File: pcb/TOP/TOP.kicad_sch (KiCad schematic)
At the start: 27 parts, among them J1 Conn_01x04, SW100 SW_DPDT_x2, SW101 SW_DPDT_x2, SW102 SW_SPDT, SW103 SW_SPDT, SW200 SW_DPDT_x2, SW201 SW_DPDT_x2, SW202 SW_SPDT, SW203 SW_SPDT

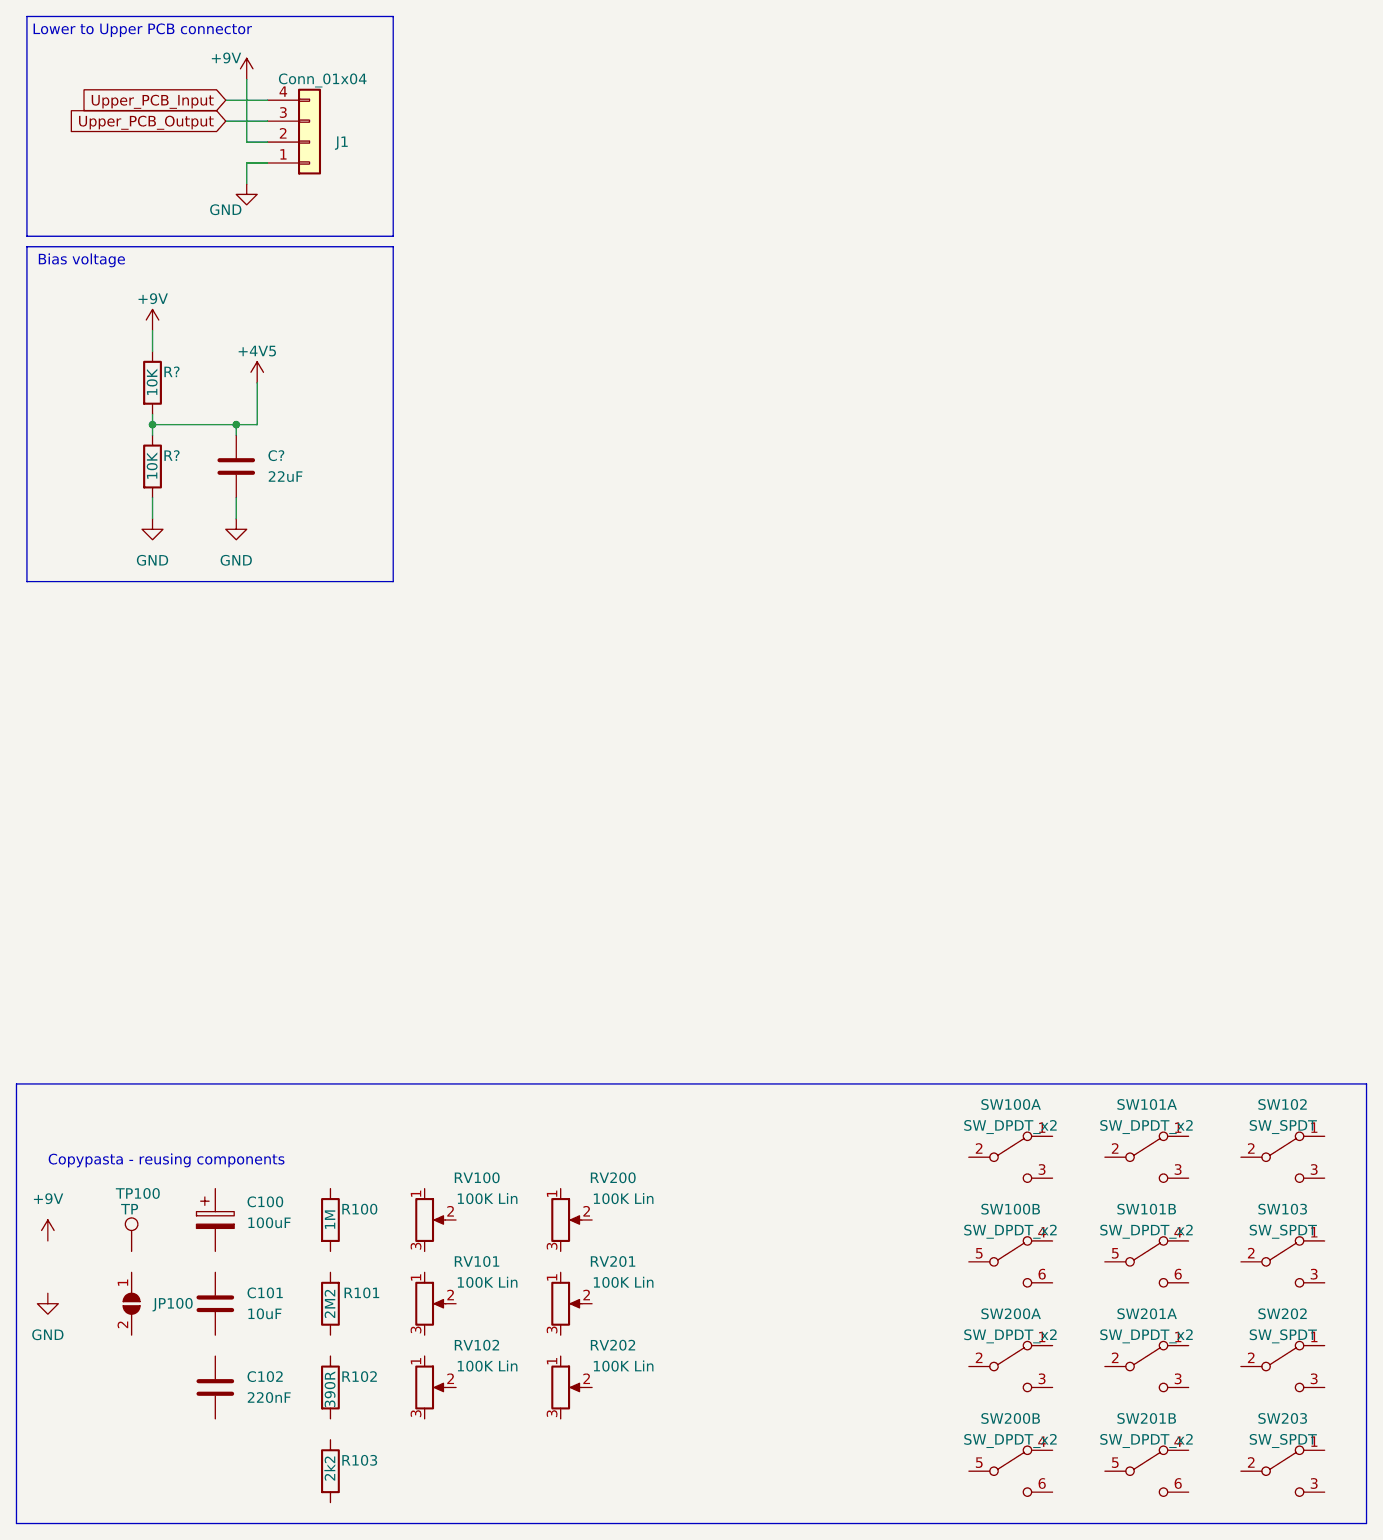
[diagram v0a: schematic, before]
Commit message: [TOP] Start schematic while debating the layout
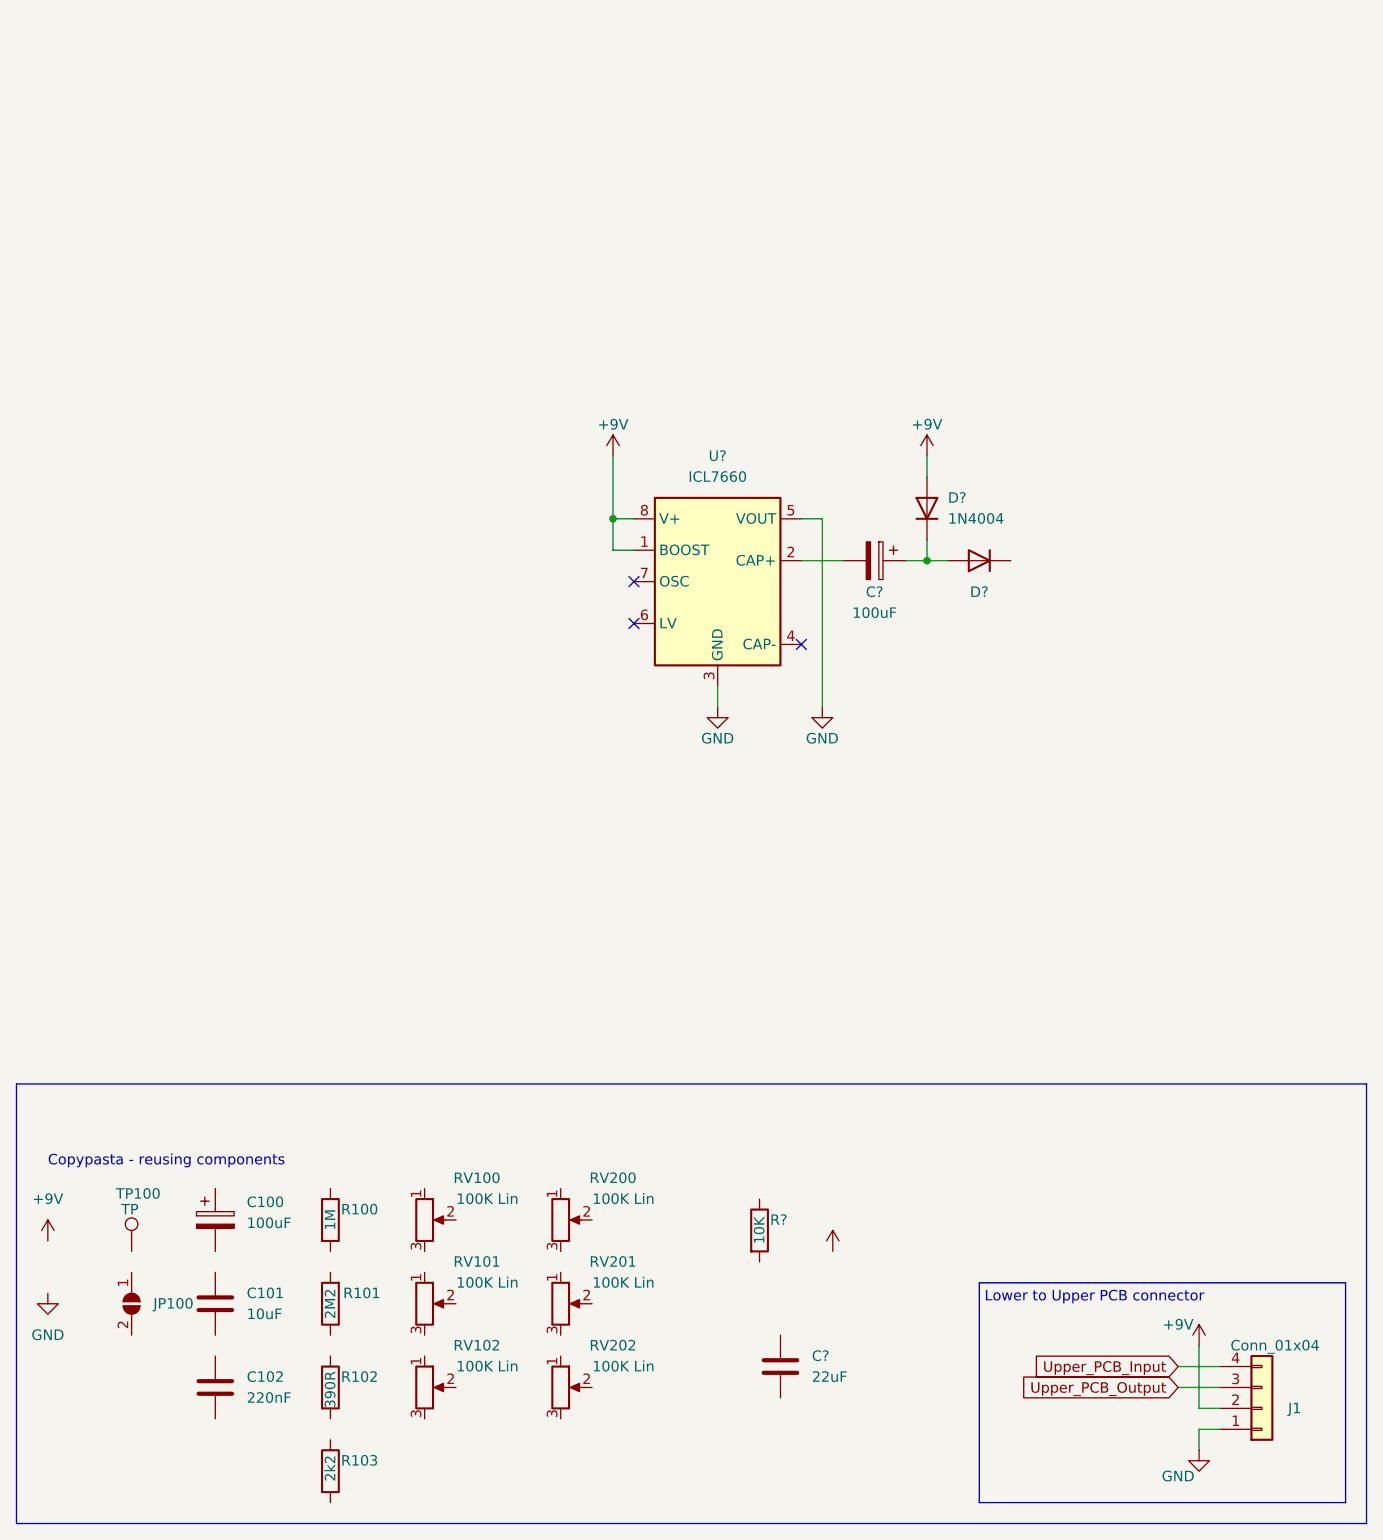
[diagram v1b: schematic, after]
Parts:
- removed R?: 10K, Resistor_SMD:R_0603_1608Metric, symbol Device:R
- removed SW100, SW101, SW200, SW201: SW_DPDT_x2, MeineBib:Switch_toggle_DPDT_Print, symbol Switch:SW_DPDT_x2
- removed SW102, SW103, SW202, SW203: SW_SPDT, MeineBib:Switch_toggle_SPDT_Print, symbol Switch:SW_SPDT
- added C?: 100uF, Capacitor_THT:CP_Radial_D5.0mm_P2.00mm, symbol Device:C_Polarized
- added D?: 1N4004, Diode_THT:D_DO-41_SOD81_P10.16mm_Horizontal, symbol Diode:1N4004
- added D?: (no value), symbol Diode:1N4004
- added U?: ICL7660, symbol Regulator_SwitchedCapacitor:ICL7660
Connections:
- net +4V5: no longer C?.1, R?.2
- net +9V: now also D?.2 (A), U?.1 (BOOST), U?.8 (V+); no longer R?.1
- net GND: now also U?.3 (GND), U?.5 (VOUT); no longer C?.2
- new net: C?.1, D?.1 (K), D?.2 (A)
- new net: C?.2, U?.2 (CAP+)
- no-connect marks 0 -> 3
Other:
- note removed: "Bias voltage"
- moved on the sheet: C?, J1, R?

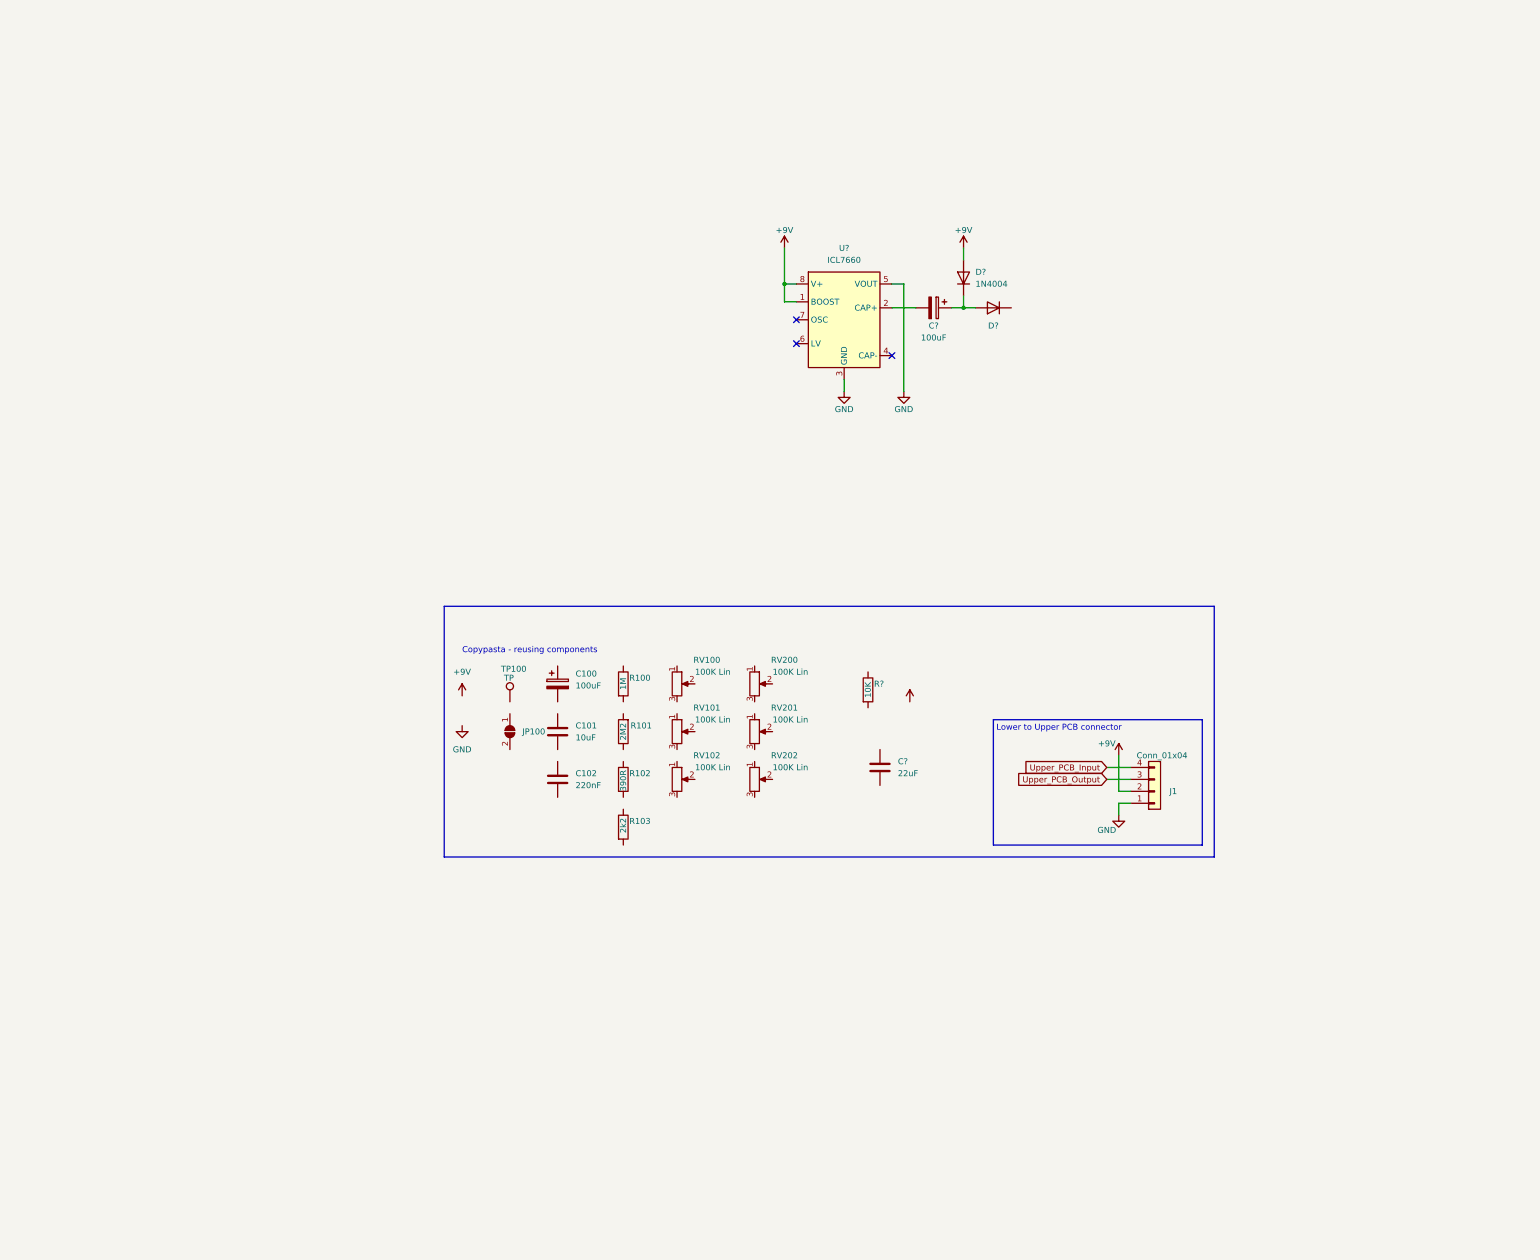
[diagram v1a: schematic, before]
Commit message: [TOP] Draw schematic input and distortion stages
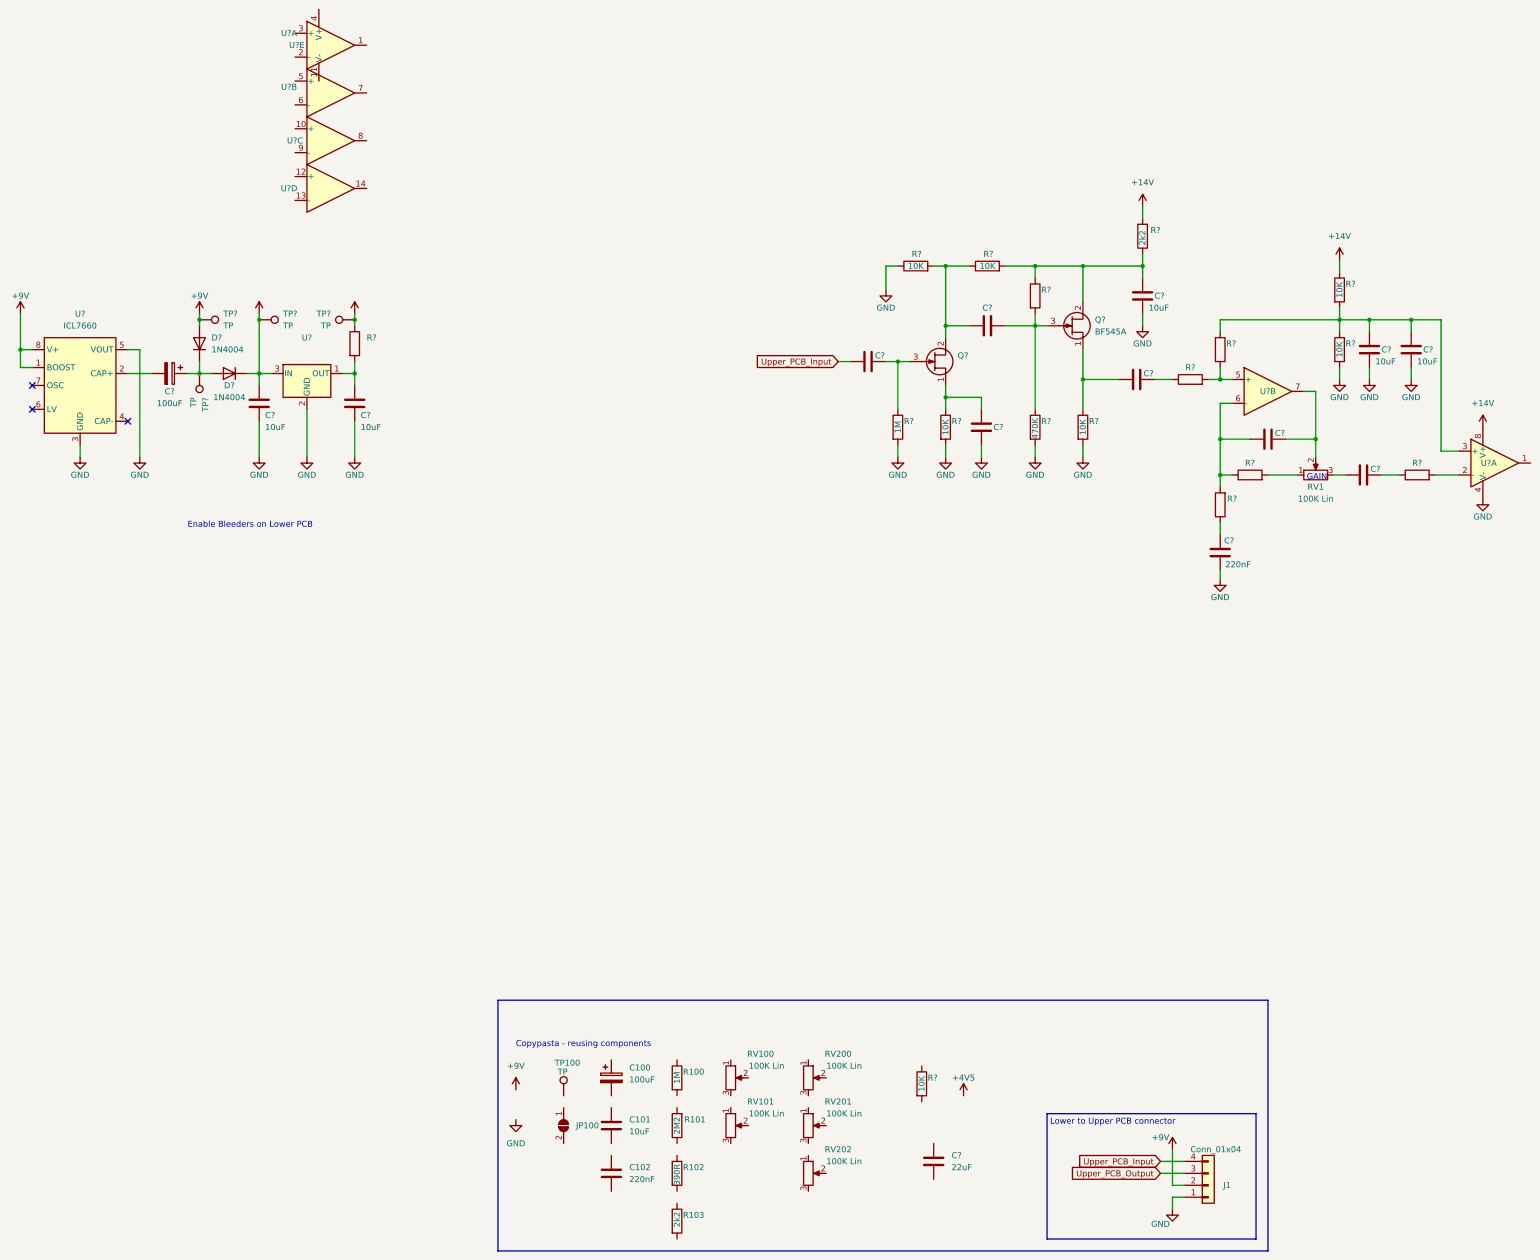
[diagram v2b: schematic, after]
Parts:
- added C? (x5): 10uF, Capacitor_SMD:C_0805_2012Metric, symbol Device:C
- added C? (x6): (no value), symbol Device:C
- added C?: 220nF, symbol Device:C
- added Q?: BF545A, Package_TO_SOT_SMD:SOT-23, symbol Transistor_FET:BF545A
- added Q?: (no value), symbol Transistor_FET:BF545A
- added R? (x7): (no value), symbol Device:R
- added R?: 2k2, Resistor_SMD:R_0603_1608Metric, symbol Device:R
- added R? (x6): 10K, Resistor_SMD:R_0603_1608Metric, symbol Device:R
- added R?: 1M, Resistor_SMD:R_0603_1608Metric, symbol Device:R
- added R?: 470K, symbol Device:R
- added TP? (x4): TP, TestPoint:TestPoint_Pad_D2.0mm, symbol Connector:TestPoint
- added U? (x5): (no value), symbol Amplifier_Operational:TL074
- added U?: (no value), symbol Regulator_Linear:L78L15_SOT89
- added U? (x3): (no value), symbol MeineBibli:OPA2604
- D?: value (none) -> 1N4004; footprint (none) -> Diode_THT:D_DO-41_SOD81_P10.16mm_Horizontal
- renumbered RV102 to RV1
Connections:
- net +4V5: now also D?.1 (K), C?.1, R?.1, R?.1, R?.2, TP?.1, TP?.1, U?.3 (IN), U?.8 (V+)
- net +9V: now also TP?.1
- net GND: now also C?.1, C?.2, C?.2, C?.2, C?.2, C?.2, C?.2, R?.1, R?.2, R?.2, R?.2, R?.2, R?.2, U?.2 (GND), U?.4 (V-)
- net Upper_PCB_Input: now also C?.2
- net at C?.1, D?.1 (K), D?.2 (A): now also TP?.1
- net at RV1.1: now also R?.2
- net at RV1.2: now also C?.1, U?.7
- net at RV1.3: now also C?.2
- new net: C?.1, R?.1 (x2)
- new net: R?.2, U?.2 (-)
- new net: C?.1, Q?.2 (D), R?.1, R?.1, R?.2
- new net: C?.1, Q?.3 (G), R?.1, R?.2
- new net: C?.1, C?.1, R?.1, R?.1, R?.2, U?.3 (+)
- new net: C?.2, Q?.1 (S), R?.1
- new net: C?.1, R?.2, U?.1 (OUT)
- new net: C?.2, R?.1, R?.2, U?.6 (-)
- new net: R?.2, R?.2, U?.5 (+)
- new net: C?.1, Q?.1 (S), R?.1
- new net: C?.2, Q?.2 (D), R?.1, R?.2
- new net: C?.2, R?.1
- new net: C?.1, Q?.3 (G), R?.1
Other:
- note added: "Enable Bleeders on Lower PCB"
- note added: "GAIN"
- moved on the sheet: C100, C101, C102, C?, D?, J1, JP100, R100, R101, R102, R103, R?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
